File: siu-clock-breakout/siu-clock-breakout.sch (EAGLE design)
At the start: 32 parts, among them IC1 ISL83485, IC2 ISL83485, IC3 ISL83485, M1 MENTOR_12701001, T1 BC847, U1 LDO-TLV1117

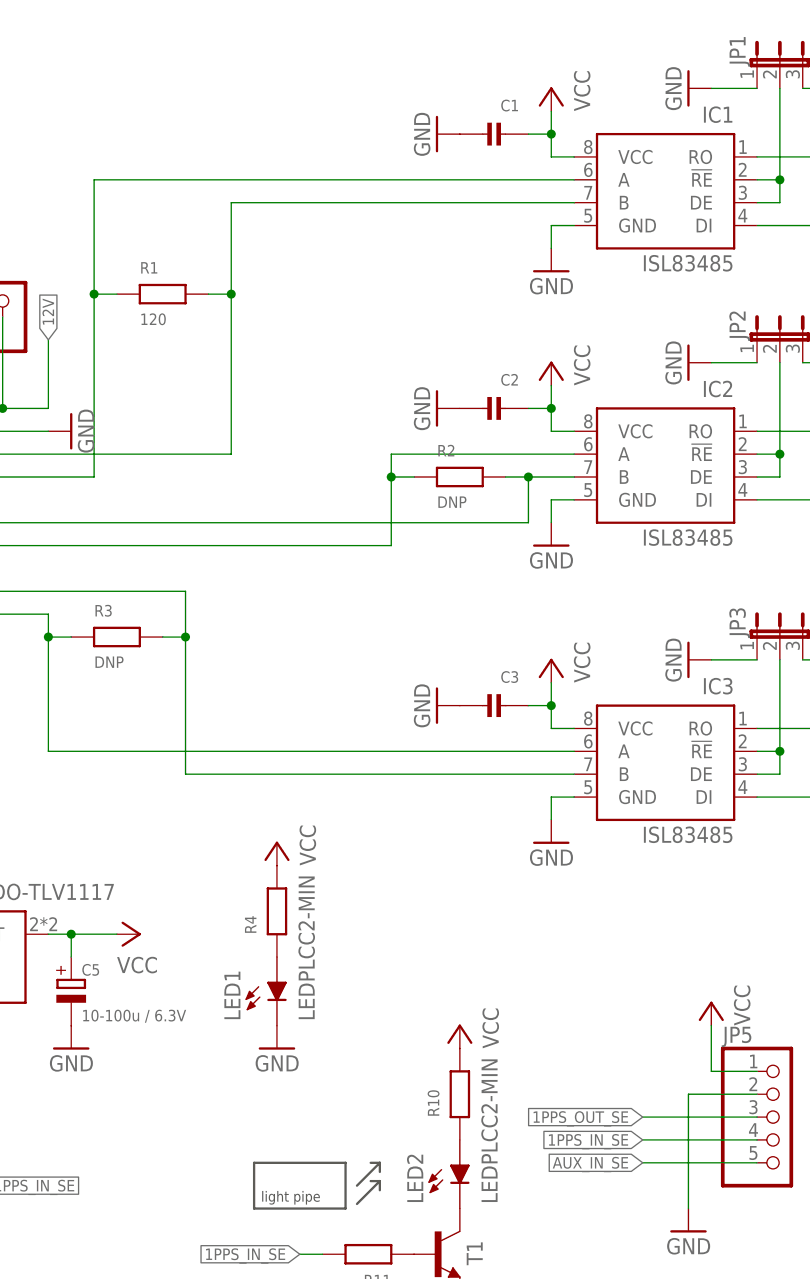
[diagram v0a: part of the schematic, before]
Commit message: siu-clock-breakout: Add missing component values
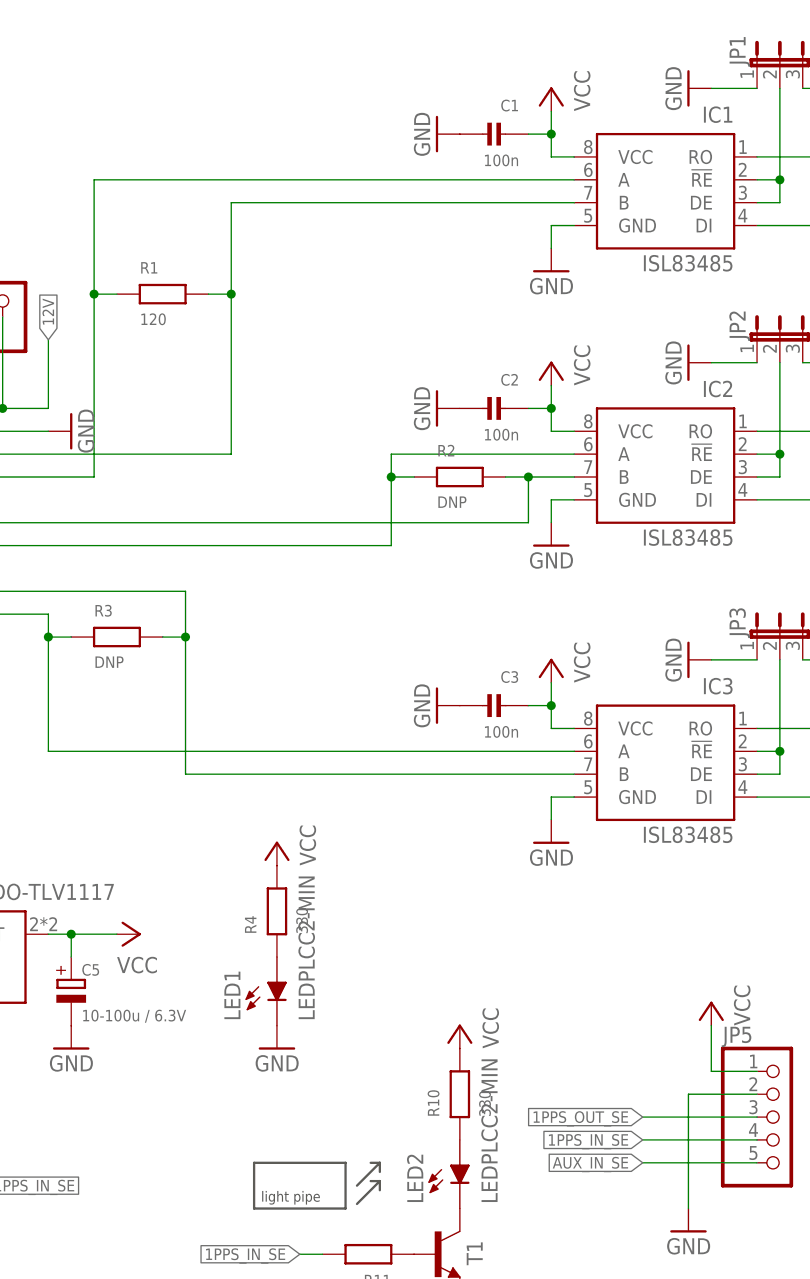
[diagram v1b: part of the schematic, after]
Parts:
- C1, C2, C3: value (none) -> 100n
- R10, R4: value (none) -> 330
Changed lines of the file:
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@@
 <part name="P+2" library="supply1" deviceset="VCC" device=""/>
 <part name="P+3" library="supply1" deviceset="VCC" device=""/>
-<part name="C1" library="rc-sysmocom" deviceset="CAP_CERAMIC" device="_0603"/>
-<part name="C2" library="rc-sysmocom" deviceset="CAP_CERAMIC" device="_0603"/>
-<part name="C3" library="rc-sysmocom" deviceset="CAP_CERAMIC" device="_0603"/>
+<part name="C1" library="rc-sysmocom" deviceset="CAP_CERAMIC" device="_0603" value="100n"/>
+<part name="C2" library="rc-sysmocom" deviceset="CAP_CERAMIC" device="_0603" value="100n"/>
+<part name="C3" library="rc-sysmocom" deviceset="CAP_CERAMIC" device="_0603" value="100n"/>
 <part name="GND4" library="supply1" deviceset="GND" device=""/>
 <part name="GND5" library="supply1" deviceset="GND" device=""/>
@@
 <part name="GND13" library="supply1" deviceset="GND" device=""/>
 <part name="LED1" library="LED-PLCC2" deviceset="LED" device="PLCC2-MIN"/>
-<part name="R4" library="rc-sysmocom" deviceset="RESISTOR" device="_0603"/>
+<part name="R4" library="rc-sysmocom" deviceset="RESISTOR" device="_0603" value="330"/>
 <part name="GND14" library="supply1" deviceset="GND" device=""/>
 <part name="P+8" library="supply1" deviceset="VCC" device=""/>
@@
 <attribute name="SOURCEPARTNUMBER" value="1727-2924-1-ND"/>
 </part>
-<part name="R10" library="rc-sysmocom" deviceset="RESISTOR" device="_0603"/>
+<part name="R10" library="rc-sysmocom" deviceset="RESISTOR" device="_0603" value="330"/>
 <part name="GND21" library="supply1" deviceset="GND" device=""/>
 <part name="P+10" library="supply1" deviceset="VCC" device=""/>
